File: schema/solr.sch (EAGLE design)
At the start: 17 parts, among them J1 ISP, U1 ATMEGA328P, U2 HMC5883L

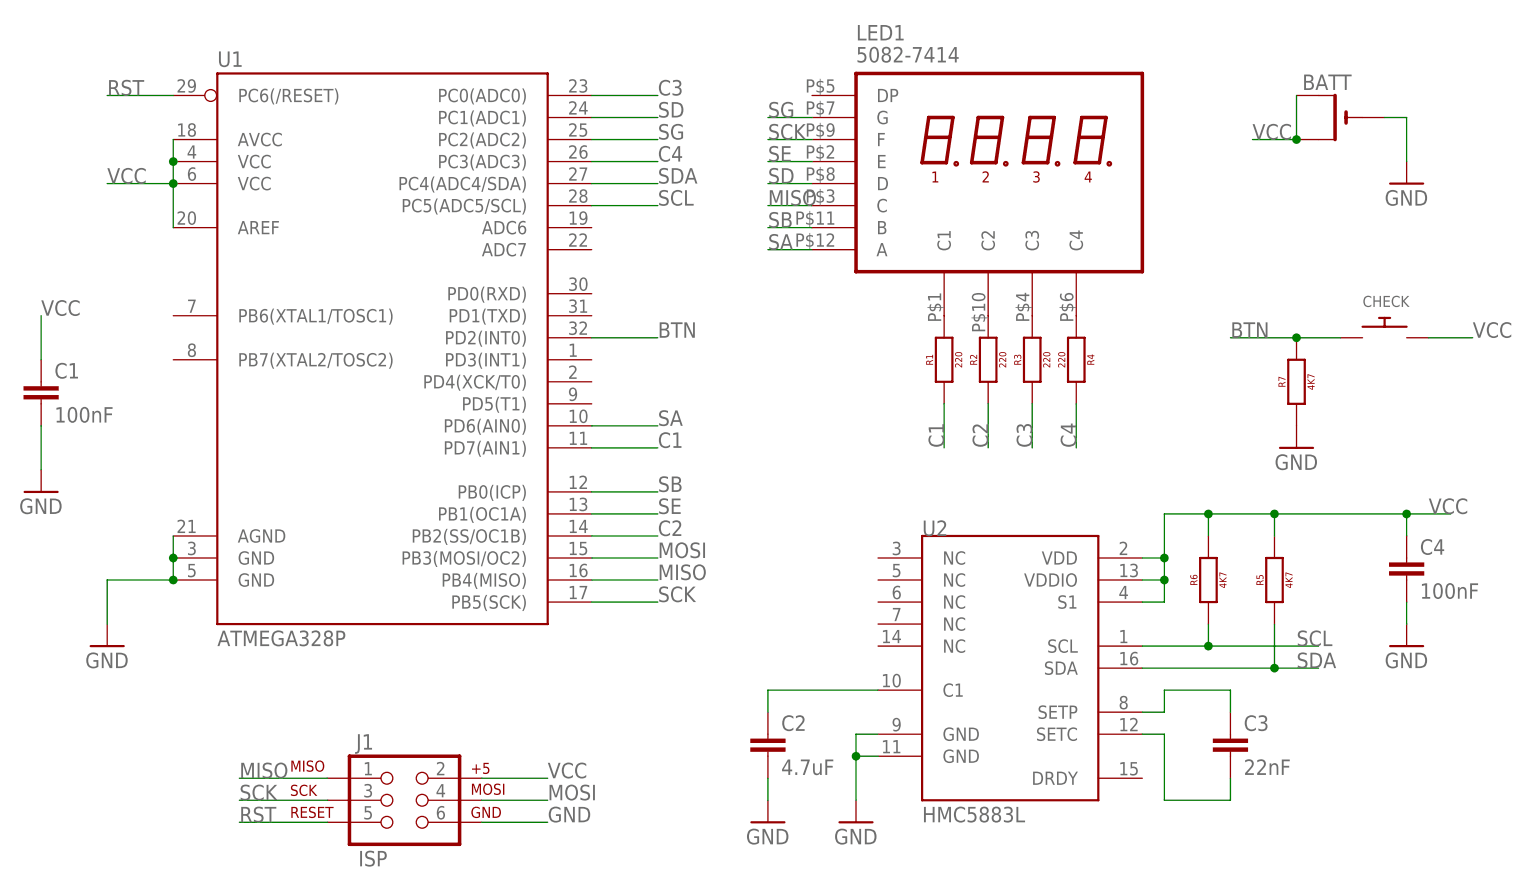
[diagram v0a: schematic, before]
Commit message: First version of the PCB sent to fab
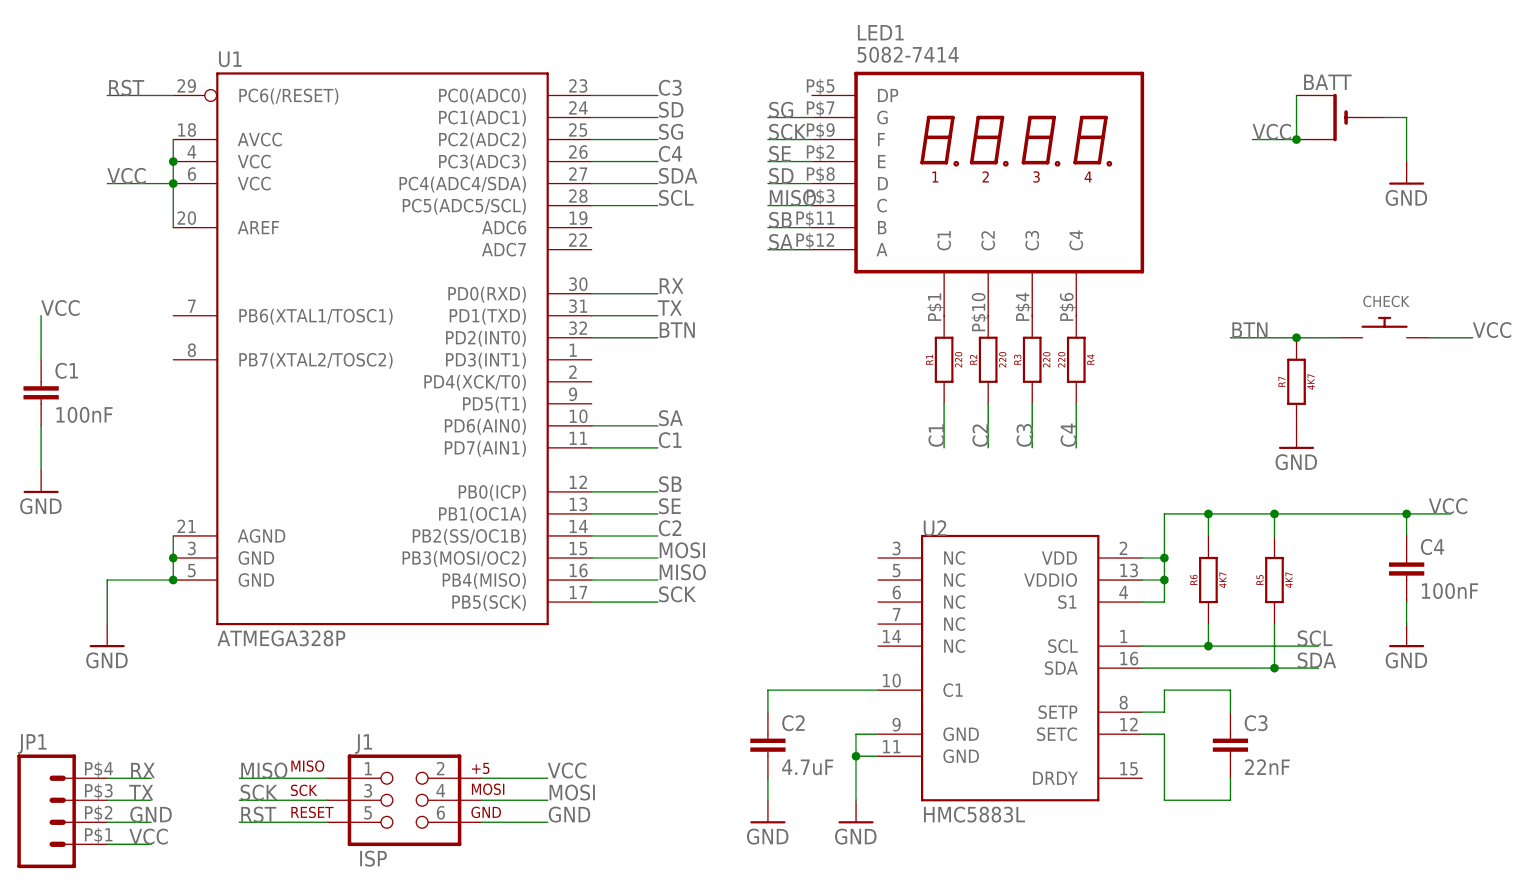
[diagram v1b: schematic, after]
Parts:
- added JP1: (no value), xose:M04SMD_ROUND_PADS
- added U$1: M3_WELDING_NUTFLAT, xose:M3_WELDING_NUTFLAT
- added U$2: M3_WELDING_NUTSTAND, xose:M3_WELDING_NUTSTAND
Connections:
- new net RX: JP1.4, U1.PD0(RXD)
- new net TX: JP1.3, U1.PD1(TXD)
- net GND: now also JP1.2
- net VCC: now also JP1.1
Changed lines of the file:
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@@
 <part name="C3" library="xose" deviceset="C-EU" device="0805" value="22nF"/>
 <part name="C4" library="xose" deviceset="C-EU" device="0805" value="100nF"/>
+<part name="JP1" library="xose" deviceset="M04" device="SMD_ROUND_PADS"/>
+<part name="U$1" library="xose" deviceset="M3_WELDING_NUT" device="FLAT"/>
+<part name="U$2" library="xose" deviceset="M3_WELDING_NUT" device="STAND"/>
 </parts>
 <sheets>
@@
 <instance part="C3" gate="G$1" x="139.7" y="15.24"/>
 <instance part="C4" gate="G$1" x="160.02" y="35.56"/>
+<instance part="JP1" gate="G$1" x="5.08" y="5.08"/>
 </instances>
 <busses>
@@
 <pinref part="U2" gate="G$1" pin="GND@1"/>
 <pinref part="U2" gate="G$1" pin="GND@2"/>
+</segment>
+<segment>
+<pinref part="JP1" gate="G$1" pin="2"/>
+<wire x1="10.16" y1="5.08" x2="15.24" y2="5.08" width="0.1524" layer="91"/>
+<label x="12.7" y="5.08" size="1.778" layer="95"/>
 </segment>
 </net>
@@
 <pinref part="C4" gate="G$1" pin="1"/>
 </segment>
+<segment>
+<pinref part="JP1" gate="G$1" pin="1"/>
+<wire x1="10.16" y1="2.54" x2="15.24" y2="2.54" width="0.1524" layer="91"/>
+<label x="12.7" y="2.54" size="1.778" layer="95"/>
+</segment>
 </net>
 <net name="SDA" class="0">
@@
 </segment>
 </net>
+<net name="RX" class="0">
+<segment>
+<pinref part="U1" gate="U$1" pin="PD0(RXD)"/>
+<wire x1="66.04" y1="66.04" x2="73.66" y2="66.04" width="0.1524" layer="91"/>
+<label x="73.66" y="66.04" size="1.778" layer="95"/>
+</segment>
+<segment>
+<pinref part="JP1" gate="G$1" pin="4"/>
+<wire x1="10.16" y1="10.16" x2="15.24" y2="10.16" width="0.1524" layer="91"/>
+<label x="12.7" y="10.16" size="1.778" layer="95"/>
+</segment>
+</net>
+<net name="TX" class="0">
+<segment>
+<pinref part="U1" gate="U$1" pin="PD1(TXD)"/>
+<wire x1="66.04" y1="63.5" x2="73.66" y2="63.5" width="0.1524" layer="91"/>
+<label x="73.66" y="63.5" size="1.778" layer="95"/>
+</segment>
+<segment>
+<pinref part="JP1" gate="G$1" pin="3"/>
+<wire x1="10.16" y1="7.62" x2="15.24" y2="7.62" width="0.1524" layer="91"/>
+<label x="12.7" y="7.62" size="1.778" layer="95"/>
+</segment>
+</net>
